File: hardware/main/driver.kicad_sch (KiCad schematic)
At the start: 10 parts, among them U501 PDSE1-S5-S24-S, U502 1EDI60N12AFXUMA1

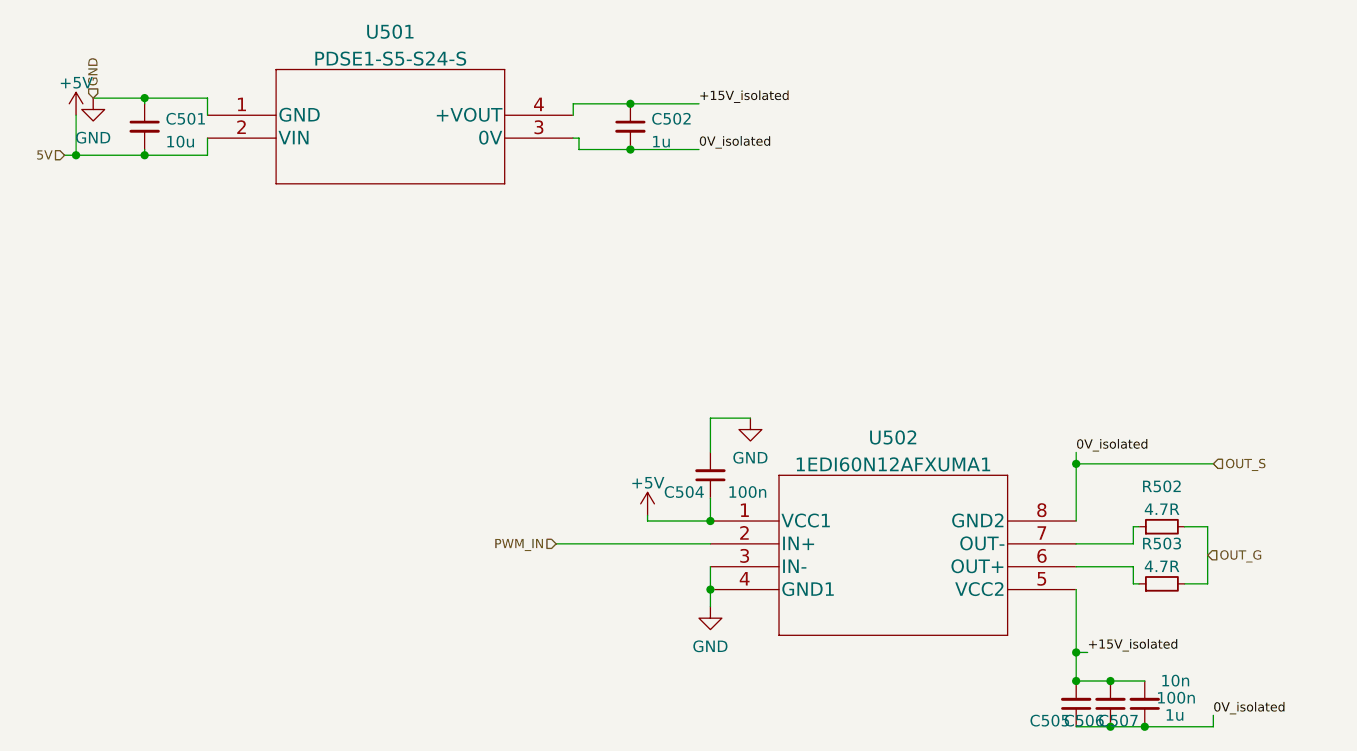
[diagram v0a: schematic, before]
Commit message: Schematics: finalize Analog Snubber and Supplies
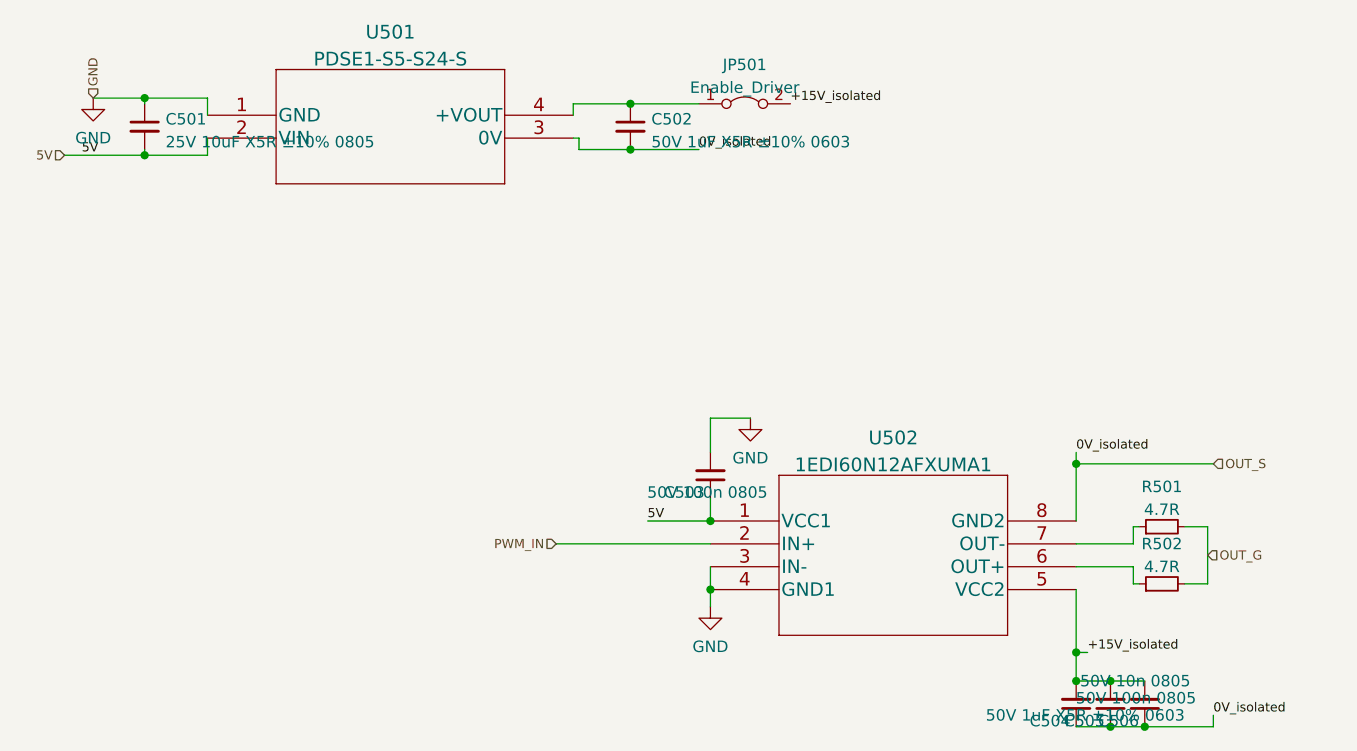
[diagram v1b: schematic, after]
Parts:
- added JP501: Enable_Driver, symbol Jumper:Jumper_2_Bridged
- C501: value 10u -> 25V 10uF X5R ±10% 0805
- C502: value 1u -> 50V 1uF X5R ±10% 0603
- C503: renamed from C504; value 100n -> 50V 100n 0805
- C504: renamed from C505; value 10n -> 50V 10n 0805
- C505: renamed from C506; value 100n -> 50V 100n 0805
- C506: renamed from C507; value 1u -> 50V 1uF X5R ±10% 0603
- U501: footprint PDSE1-S_11.60x6.00x10.16_CUI -> (none)
- U502: footprint PG-DSO-8_3P9X4P9_INF -> (none)
- renumbered R502 to R501, R503 to R502
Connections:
- net +15V_isolated: now also JP501.2 (B); no longer C502.1, U501.4 (+VOUT)
- net +5V renamed 5V
- new net: C502.1, JP501.1 (A), U501.4 (+VOUT)
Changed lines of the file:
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@@
   (junction (at 153.035 128.905) (diameter 0) (color 0 0 0 0)
   )
-  (junction (at 41.91 70.485) (diameter 0) (color 0 0 0 0)
-  )
   (junction (at 156.845 133.985) (diameter 0) (color 0 0 0 0)
   )
@@
     (stroke (width 0) (type default) (color 0 0 0 0))
   )
-  (wire (pts (xy 41.91 70.485) (xy 49.53 70.485))
-    (stroke (width 0) (type default) (color 0 0 0 0))
-  )
-  (wire (pts (xy 41.91 66.04) (xy 41.91 70.485))
+  (wire (pts (xy 40.64 70.485) (xy 49.53 70.485))
     (stroke (width 0) (type default) (color 0 0 0 0))
   )
@@
     (stroke (width 0) (type default) (color 0 0 0 0))
   )
-  (wire (pts (xy 40.64 70.485) (xy 41.91 70.485))
-    (stroke (width 0) (type default) (color 0 0 0 0))
-  )
   (wire (pts (xy 112.395 103.505) (xy 112.395 99.695))
     (stroke (width 0) (type default) (color 0 0 0 0))
@@
     (stroke (width 0) (type default) (color 0 0 0 0))
   )
-  (wire (pts (xy 105.41 111.125) (xy 105.41 110.49))
-    (stroke (width 0) (type default) (color 0 0 0 0))
-  )
   (wire (pts (xy 153.035 116.205) (xy 159.385 116.205))
     (stroke (width 0) (type default) (color 0 0 0 0))
@@
     (stroke (width 0) (type default) (color 0 0 0 0))
   )
-  (label "+15V_isolated" (at 111.125 64.77 0)
+  (label "5V" (at 105.41 111.125 0)
+    (effects (font (size 1.016 1.016)) (justify left bottom))
+  )
+  (label "+15V_isolated" (at 121.285 64.77 0)
+    (effects (font (size 1.016 1.016)) (justify left bottom))
+  )
+  (label "5V" (at 42.545 70.485 0)
     (effects (font (size 1.016 1.016)) (justify left bottom))
   )
@@
       (effects (font (size 1.27 1.27)) (justify left))
     )
-    (property "Value" "1u" (id 1) (at 105.8291 69.0185 0)
+    (property "Value" "50V 1uF X5R ±10% 0603" (id 1) (at 105.8291 69.0185 0)
       (effects (font (size 1.27 1.27)) (justify left))
     )
@@
   (symbol (lib_id "Device:R_Small") (at 162.56 118.11 90) (unit 1)
     (in_bom yes) (on_board yes) (fields_autoplaced)
-    (property "Reference" "R503" (id 0) (at 162.56 113.6736 90))
+    (property "Reference" "R502" (id 0) (at 162.56 113.6736 90))
     (property "Value" "4.7R" (id 1) (at 162.56 116.2105 90))
     (property "Footprint" "" (id 2) (at 162.56 118.11 0)
@@
     (pin "2")
   )
-  (symbol (lib_id "power:+5V") (at 105.41 110.49 0) (unit 1)
-    (in_bom yes) (on_board yes) (fields_autoplaced)
-    (property "Reference" "#PWR0178" (id 0) (at 105.41 114.3 0)
-      (effects (font (size 1.27 1.27)) hide)
-    )
-    (property "Value" "+5V" (id 1) (at 105.41 106.9142 0))
-    (property "Footprint" "" (id 2) (at 105.41 110.49 0)
-      (effects (font (size 1.27 1.27)) hide)
-    )
-    (property "Datasheet" "" (id 3) (at 105.41 110.49 0)
-      (effects (font (size 1.27 1.27)) hide)
-    )
-    (pin "1")
-  )
-  (symbol (lib_id "power:+5V") (at 41.91 66.04 0) (unit 1)
-    (in_bom yes) (on_board yes) (fields_autoplaced)
-    (property "Reference" "#PWR0174" (id 0) (at 41.91 69.85 0)
-      (effects (font (size 1.27 1.27)) hide)
-    )
-    (property "Value" "+5V" (id 1) (at 41.91 62.4642 0))
-    (property "Footprint" "" (id 2) (at 41.91 66.04 0)
-      (effects (font (size 1.27 1.27)) hide)
-    )
-    (property "Datasheet" "" (id 3) (at 41.91 66.04 0)
-      (effects (font (size 1.27 1.27)) hide)
-    )
-    (pin "1")
-  )
   (symbol (lib_id "Device:C_Small") (at 49.53 67.31 0) (unit 1)
     (in_bom yes) (on_board yes) (fields_autoplaced)
@@
       (effects (font (size 1.27 1.27)) (justify left))
     )
-    (property "Value" "10u" (id 1) (at 51.8541 69.0185 0)
+    (property "Value" "25V 10uF X5R ±10% 0805" (id 1) (at 51.8541 69.0185 0)
       (effects (font (size 1.27 1.27)) (justify left))
     )
@@
   (symbol (lib_id "power:GND") (at 116.84 99.695 0) (unit 1)
     (in_bom yes) (on_board yes) (fields_autoplaced)
-    (property "Reference" "#PWR0177" (id 0) (at 116.84 106.045 0)
+    (property "Reference" "#PWR0503" (id 0) (at 116.84 106.045 0)
       (effects (font (size 1.27 1.27)) hide)
     )
@@
   (symbol (lib_id "Device:R_Small") (at 162.56 111.76 90) (unit 1)
     (in_bom yes) (on_board yes) (fields_autoplaced)
-    (property "Reference" "R502" (id 0) (at 162.56 107.3236 90))
+    (property "Reference" "R501" (id 0) (at 162.56 107.3236 90))
     (property "Value" "4.7R" (id 1) (at 162.56 109.8605 90))
     (property "Footprint" "" (id 2) (at 162.56 111.76 0)
@@
   (symbol (lib_id "power:GND") (at 112.395 120.65 0) (unit 1)
     (in_bom yes) (on_board yes) (fields_autoplaced)
-    (property "Reference" "#PWR0176" (id 0) (at 112.395 127 0)
+    (property "Reference" "#PWR0502" (id 0) (at 112.395 127 0)
       (effects (font (size 1.27 1.27)) hide)
     )
@@
     (pin "1")
   )
+  (symbol (lib_id "Jumper:Jumper_2_Bridged") (at 116.205 64.77 0) (unit 1)
+    (in_bom yes) (on_board yes) (fields_autoplaced)
+    (property "Reference" "JP501" (id 0) (at 116.205 60.4352 0))
+    (property "Value" "Enable_Driver" (id 1) (at 116.205 62.9721 0))
+    (property "Footprint" "" (id 2) (at 116.205 64.77 0)
+      (effects (font (size 1.27 1.27)) hide)
+    )
+    (property "Datasheet" "~" (id 3) (at 116.205 64.77 0)
+      (effects (font (size 1.27 1.27)) hide)
+    )
+    (pin "1")
+    (pin "2")
+  )
   (symbol (lib_id "Device:C_Small") (at 156.845 131.445 180) (unit 1)
     (in_bom yes) (on_board yes)
-    (property "Reference" "C506" (id 0) (at 156.21 133.35 0)
-      (effects (font (size 1.27 1.27)) (justify left))
-    )
-    (property "Value" "100n" (id 1) (at 166.37 130.81 0)
+    (property "Reference" "C505" (id 0) (at 156.21 133.35 0)
+      (effects (font (size 1.27 1.27)) (justify left))
+    )
+    (property "Value" "50V 100n 0805" (id 1) (at 166.37 130.81 0)
       (effects (font (size 1.27 1.27)) (justify left))
     )
@@
   (symbol (lib_id "Device:C_Small") (at 160.655 131.445 180) (unit 1)
     (in_bom yes) (on_board yes)
-    (property "Reference" "C507" (id 0) (at 160.02 133.35 0)
-      (effects (font (size 1.27 1.27)) (justify left))
-    )
-    (property "Value" "1u" (id 1) (at 165.1 132.715 0)
+    (property "Reference" "C506" (id 0) (at 160.02 133.35 0)
+      (effects (font (size 1.27 1.27)) (justify left))
+    )
+    (property "Value" "50V 1uF X5R ±10% 0603" (id 1) (at 165.1 132.715 0)
       (effects (font (size 1.27 1.27)) (justify left))
     )
@@
   (symbol (lib_id "power:GND") (at 43.815 64.135 0) (unit 1)
     (in_bom yes) (on_board yes) (fields_autoplaced)
-    (property "Reference" "#PWR0175" (id 0) (at 43.815 70.485 0)
+    (property "Reference" "#PWR0501" (id 0) (at 43.815 70.485 0)
       (effects (font (size 1.27 1.27)) hide)
     )
@@
       (effects (font (size 1.524 1.524)))
     )
-    (property "Footprint" "PG-DSO-8_3P9X4P9_INF" (id 2) (at 132.715 105.029 0)
+    (property "Footprint" "" (id 2) (at 132.715 105.029 0)
       (effects (font (size 1.524 1.524)) hide)
     )
@@
       (effects (font (size 1.524 1.524)))
     )
-    (property "Footprint" "PDSE1-S_11.60x6.00x10.16_CUI" (id 2) (at 76.835 59.944 0)
+    (property "Footprint" "" (id 2) (at 76.835 59.944 0)
       (effects (font (size 1.524 1.524)) hide)
     )
@@
   (symbol (lib_id "Device:C_Small") (at 153.035 131.445 180) (unit 1)
     (in_bom yes) (on_board yes)
-    (property "Reference" "C505" (id 0) (at 152.4 133.35 0)
-      (effects (font (size 1.27 1.27)) (justify left))
-    )
-    (property "Value" "10n" (id 1) (at 165.735 128.905 0)
+    (property "Reference" "C504" (id 0) (at 152.4 133.35 0)
+      (effects (font (size 1.27 1.27)) (justify left))
+    )
+    (property "Value" "50V 10n 0805" (id 1) (at 165.735 128.905 0)
       (effects (font (size 1.27 1.27)) (justify left))
     )
@@
   (symbol (lib_id "Device:C_Small") (at 112.395 106.045 180) (unit 1)
     (in_bom yes) (on_board yes)
-    (property "Reference" "C504" (id 0) (at 111.76 107.95 0)
-      (effects (font (size 1.27 1.27)) (justify left))
-    )
-    (property "Value" "100n" (id 1) (at 118.745 107.95 0)
-      (effects (font (size 1.27 1.27)) (justify left))
-    )
+    (property "Reference" "C503" (id 0) (at 111.76 107.95 0)
+      (effects (font (size 1.27 1.27)) (justify left))
+    )
+    (property "Value" "50V 100n 0805" (id 1) (at 118.745 107.95 0)
+      (effects (font (size 1.27 1.27)) (justify left))
+    )

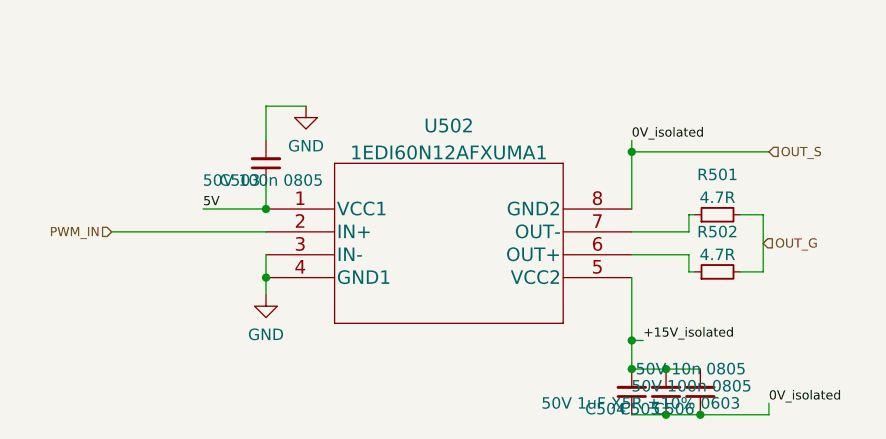
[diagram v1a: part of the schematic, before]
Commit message: Schematics: Modified component values
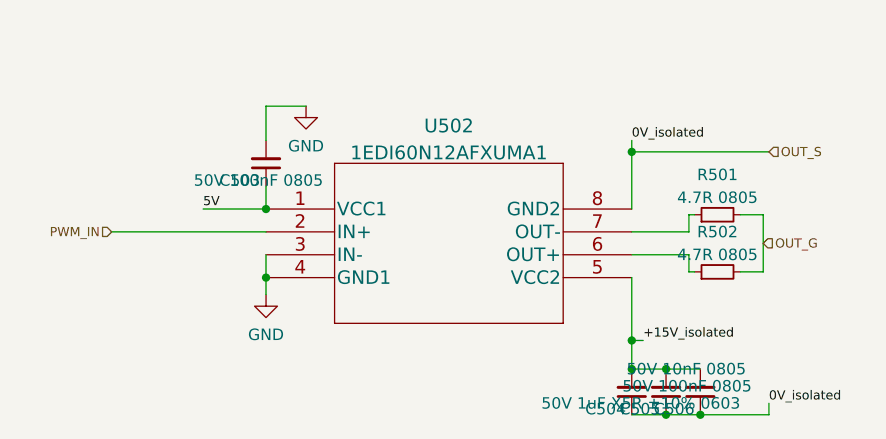
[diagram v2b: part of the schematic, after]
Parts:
- C503, C505: value 50V 100n 0805 -> 50V 100nF 0805
- C504: value 50V 10n 0805 -> 50V 10nF 0805
- R501, R502: value 4.7R -> 4.7R 0805
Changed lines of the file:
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@@
     (in_bom yes) (on_board yes) (fields_autoplaced)
     (property "Reference" "R502" (id 0) (at 162.56 113.6736 90))
-    (property "Value" "4.7R" (id 1) (at 162.56 116.2105 90))
+    (property "Value" "4.7R 0805" (id 1) (at 162.56 116.2105 90))
     (property "Footprint" "" (id 2) (at 162.56 118.11 0)
       (effects (font (size 1.27 1.27)) hide)
@@
     (in_bom yes) (on_board yes) (fields_autoplaced)
     (property "Reference" "R501" (id 0) (at 162.56 107.3236 90))
-    (property "Value" "4.7R" (id 1) (at 162.56 109.8605 90))
+    (property "Value" "4.7R 0805" (id 1) (at 162.56 109.8605 90))
     (property "Footprint" "" (id 2) (at 162.56 111.76 0)
       (effects (font (size 1.27 1.27)) hide)
@@
       (effects (font (size 1.27 1.27)) (justify left))
     )
-    (property "Value" "50V 100n 0805" (id 1) (at 166.37 130.81 0)
+    (property "Value" "50V 100nF 0805" (id 1) (at 166.37 130.81 0)
       (effects (font (size 1.27 1.27)) (justify left))
     )
@@
       (effects (font (size 1.27 1.27)) (justify left))
     )
-    (property "Value" "50V 10n 0805" (id 1) (at 165.735 128.905 0)
+    (property "Value" "50V 10nF 0805" (id 1) (at 165.735 128.905 0)
       (effects (font (size 1.27 1.27)) (justify left))
     )
@@
       (effects (font (size 1.27 1.27)) (justify left))
     )
-    (property "Value" "50V 100n 0805" (id 1) (at 118.745 107.95 0)
+    (property "Value" "50V 100nF 0805" (id 1) (at 118.745 107.95 0)
       (effects (font (size 1.27 1.27)) (justify left))
     )

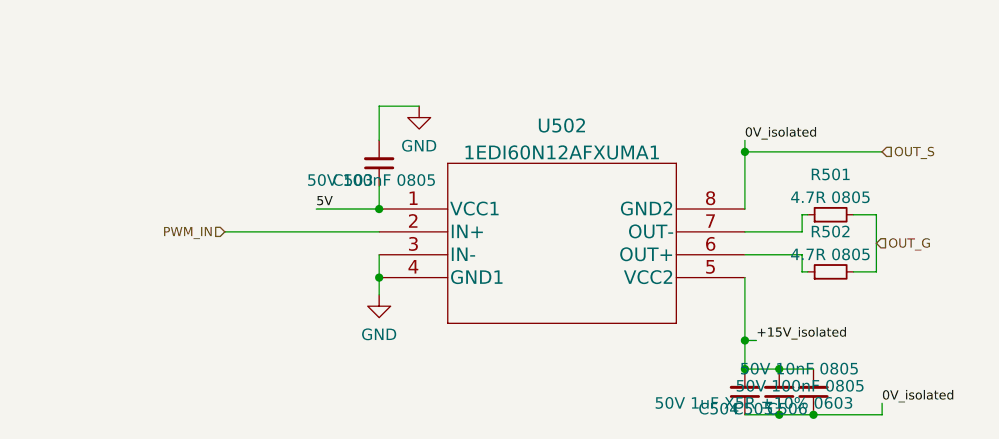
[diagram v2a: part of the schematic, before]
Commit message: Schematics: Sym table and libs updated
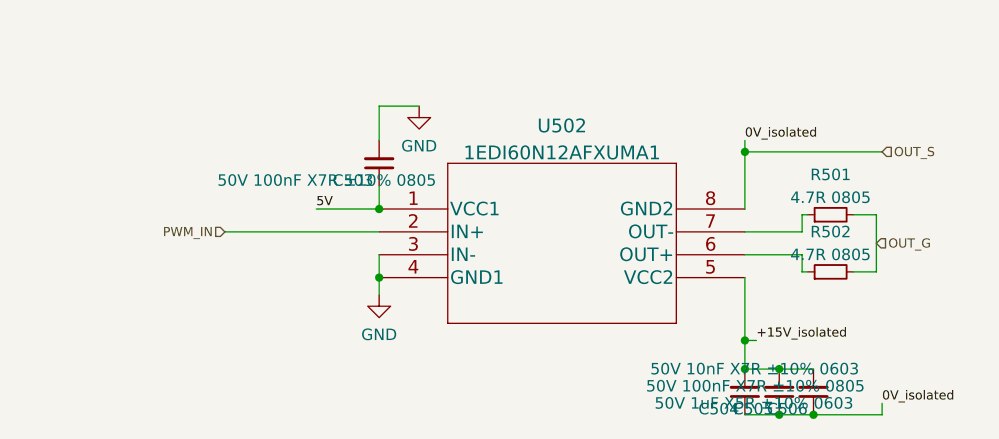
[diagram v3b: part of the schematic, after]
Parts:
- C503, C505: value 50V 100nF 0805 -> 50V 100nF X7R ±10% 0805
- C504: value 50V 10nF 0805 -> 50V 10nF X7R ±10% 0603
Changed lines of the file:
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@@
       (effects (font (size 1.27 1.27)) (justify left))
     )
-    (property "Value" "50V 100nF 0805" (id 1) (at 166.37 130.81 0)
+    (property "Value" "50V 100nF X7R ±10% 0805" (id 1) (at 166.37 130.81 0)
       (effects (font (size 1.27 1.27)) (justify left))
     )
@@
       (effects (font (size 1.27 1.27)) (justify left))
     )
-    (property "Value" "50V 10nF 0805" (id 1) (at 165.735 128.905 0)
+    (property "Value" "50V 10nF X7R ±10% 0603" (id 1) (at 165.735 128.905 0)
       (effects (font (size 1.27 1.27)) (justify left))
     )
@@
       (effects (font (size 1.27 1.27)) (justify left))
     )
-    (property "Value" "50V 100nF 0805" (id 1) (at 118.745 107.95 0)
+    (property "Value" "50V 100nF X7R ±10% 0805" (id 1) (at 118.745 107.95 0)
       (effects (font (size 1.27 1.27)) (justify left))
     )
